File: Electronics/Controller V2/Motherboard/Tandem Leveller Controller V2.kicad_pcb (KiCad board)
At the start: 2 copper layers, 13 parts, among them J1 Conn_01x08, J2 Conn_01x10, J3 GNSS, U2 simpleRTK2B

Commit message: WIP
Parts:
- added C1: 100n, Capacitor_SMD:C_0805_2012Metric, F.Cu at (250.4, 66.3)
- added C10: 100n, Capacitor_SMD:C_0805_2012Metric, F.Cu at (102.7, -32.0)
- added C11: 560u, Capacitor_SMD:CP_Elec_10x10.5, F.Cu at (117.4, -65.3)
- added C12: 560u, Capacitor_SMD:CP_Elec_10x10.5, F.Cu at (117.4, -53.2)
- added C2: 100n, Capacitor_SMD:C_0805_2012Metric, F.Cu at (250.4, 69.3)
- added C3: 100n, Capacitor_SMD:C_0805_2012Metric, F.Cu at (99.2, -7.16)
- added C4: 100n, Capacitor_SMD:C_0805_2012Metric, F.Cu at (99.2, -4.15)
- added C5: 680u, Capacitor_SMD:CP_Elec_10x10.5, F.Cu at (117.4, -77.3)
- added C6: 220u, Capacitor_SMD:CP_Elec_8x6.5, F.Cu at (98.4, -41.4)
- added C7: 1729034, Capacitor_SMD:CP_Elec_6.3x5.9, F.Cu at (145.4, -79.3)
- added C8: 1729034, Capacitor_SMD:CP_Elec_6.3x5.9, F.Cu at (145.4, -71.2)
- added C9: 100n, Capacitor_SMD:C_0805_2012Metric, F.Cu at (102.7, -35.0)
- added D1: APTD1608SECK, Diode_SMD:D_0603_1608Metric, F.Cu at (102.5, -29.2)
- added D2: B360A-13-F, Diode_SMD:D_SMA, F.Cu at (96.4, -34.2)
- added D3: PDS760-13, Diode_SMD:D_PowerDI-5, F.Cu at (118.8, -44.4)
- added D4: PDS760-13, Diode_SMD:D_PowerDI-5, F.Cu at (118.8, -38.8)
- added F1: 10A, Britishideas:5x20 Fuse Holder, F.Cu at (126.0, -38.0)
- added J14: TABLET 1 PWR, Connector_BarrelJack:BarrelJack_Wuerth_6941xx301002, F.Cu at (130.1, -54.0)
- added J15: TABLET 2 PWR, Connector_BarrelJack:BarrelJack_Wuerth_6941xx301002, F.Cu at (142.4, -54.0)
- added J4: TERM, Connector_PinHeader_2.54mm:PinHeader_1x02_P2.54mm_Vertical, F.Cu at (94.7, -6.34)
- added J5: Pulse_J0011D01BNL, EmSA:Pulse_J0011D01BNL, F.Cu at (240.0, 62.3)
- added J6: CAN, Connector_Dsub:DSUB-9_Male_Vertical_P2.77x2.84mm, F.Cu at (107.5, -19.9)
- added J7: Pulse_J0011D01BNL, EmSA:Pulse_J0011D01BNL, F.Cu at (258.8, 62.3)
- added L1: ACT1210-510-2P-TL00, EmSA:ACT1210-510-2P-TL00, F.Cu at (108.4, -6.86)
- added L2: 33uH, Britishideas:MWSA0603S-330MT, F.Cu at (116.1, -32.1)
- added L3: MWSA1206S-470MT, Britishideas:MWSA1206S-470MT, F.Cu at (126.7, -76.5)
- added L4: MWSA1206S-470MT, Britishideas:MWSA1206S-470MT, F.Cu at (126.7, -62.8)
- added R1: 1k, Resistor_SMD:R_0805_2012Metric, F.Cu at (237.2, 66.2)
- added R10: 1k, Resistor_SMD:R_0805_2012Metric, F.Cu at (246.0, 69.2)
- added R11: 1k, Resistor_SMD:R_0805_2012Metric, F.Cu at (246.0, 72.1)
- added R12: 330, Resistor_SMD:R_0805_2012Metric, F.Cu at (112.2, -45.8)
- added R13: 10k, Resistor_SMD:R_0805_2012Metric, F.Cu at (103.6, -7.19)
- added R14: 120, Resistor_SMD:R_0805_2012Metric, F.Cu at (103.6, -4.24)
- added R15: 3k, Resistor_SMD:R_0805_2012Metric, F.Cu at (112.2, -42.8)
- added R16: 3k, Resistor_SMD:R_0805_2012Metric, F.Cu at (112.2, -39.9)
- added R17: 1k, Resistor_SMD:R_0805_2012Metric, F.Cu at (246.0, 75.1)
- added R18: 18k, Resistor_SMD:R_0805_2012Metric, F.Cu at (112.2, -36.9)
- added R19: 1k5, Resistor_SMD:R_0805_2012Metric, F.Cu at (112.2, -34.0)
- added R2: 1k, Resistor_SMD:R_0805_2012Metric, F.Cu at (237.2, 69.2)
- added R20: 18k, Resistor_SMD:R_0805_2012Metric, F.Cu at (112.2, -31.0)
- added R21: 1k5, Resistor_SMD:R_0805_2012Metric, F.Cu at (112.2, -28.1)
- added R3: 1k, Resistor_SMD:R_0805_2012Metric, F.Cu at (237.2, 72.1)
- added R4: 1k, Resistor_SMD:R_0805_2012Metric, F.Cu at (237.2, 75.1)
- added R5: 1k, Resistor_SMD:R_0805_2012Metric, F.Cu at (241.6, 66.2)
- added R6: 1k, Resistor_SMD:R_0805_2012Metric, F.Cu at (241.6, 69.2)
- added R7: 1k, Resistor_SMD:R_0805_2012Metric, F.Cu at (241.6, 72.1)
- added R8: 1k, Resistor_SMD:R_0805_2012Metric, F.Cu at (241.6, 75.1)
- added R9: 1k, Resistor_SMD:R_0805_2012Metric, F.Cu at (246.0, 66.2)
- added U10: LM2587S-ADJ/NOPB, Package_TO_SOT_SMD:TO-263-5_TabPin6, F.Cu at (103.1, -52.5)
- added U3: Adafruit BNO085, Britishideas:Adafruit_BNO085, F.Cu at (25.2, 63.8)
- added U4: ~, Britishideas:Teensy_4.1, F.Cu at (198.6, 43.8)
- added U5: ~, Britishideas:Teensy_4.1, F.Cu at (217.7, 43.8)
- added U6: TJA1462ATK-0Z, EmSA:HVSON8_0_65mm, F.Cu at (117.1, -5.18)
- added U7: PESD2CANFD24V-TR, Package_TO_SOT_SMD:SOT-23, F.Cu at (113.4, -6.44)
- added U8: LM2596S-5, Package_TO_SOT_SMD:TO-263-5_TabPin3, F.Cu at (103.1, -77.2)
- added U9: LM2587S-ADJ/NOPB, Package_TO_SOT_SMD:TO-263-5_TabPin6, F.Cu at (103.1, -64.8)
- moved H1 63.1 mm to (123.1, 91.2)
- moved H2 63.1 mm to (177.6, 91.2)
- moved H3 63.1 mm to (177.6, 155.7)
- moved H4 63.1 mm to (123.1, 155.7)
- moved J1 63.1 mm to (175.1, 101.2)
- moved J2 63.1 mm to (133.1, 123.2)
- moved U1 63.1 mm to (162.9, 90.7)
- moved H7 22.5 mm to (28.5, 155.1)
- moved U2 22.5 mm to (38.0, 93.1)
- moved H5 22.5 mm to (28.5, 94.6)
- moved H8 22.5 mm to (103.0, 155.1)
- moved J3 22.5 mm to (92.5, 145.6)
- moved H6 22.5 mm to (103.0, 94.6)
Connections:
- U1 pad 1: /Valves/VALVE_A_DIR -> /MCUs/VALVE_A_DIR
- U1 pad 2: /Valves/VALVE_A_PWM -> /MCUs/VALVE_A_PWM

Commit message: Added AMP connectors. Working on PCB layout.
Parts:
- added J8: 776180-1, Britishideas:776180-1 AMPHENOL AMP 35pos, F.Cu at (221.9, 114.0)
- added J9: 776279-1, Britishideas:776279-1 AMPHENOL AMP 8pos, F.Cu at (221.9, 36.7)
- moved U5 312.9 mm to (527.5, 87.9), turned to 180 degrees
- moved C1 296.9 mm to (547.3, 61.1)
- moved C2 296.9 mm to (547.3, 64.1)
- moved C3 296.9 mm to (396.1, -12.4)
- moved C4 296.9 mm to (396.1, -9.35)
- moved C6 296.9 mm to (395.3, -46.6)
- moved H5 296.9 mm to (325.4, 89.4)
- moved H7 296.9 mm to (325.4, 149.9)
- moved J6 296.9 mm to (404.4, -25.1)
- moved L1 296.9 mm to (405.3, -12.1)
- moved R1 296.9 mm to (534.1, 61.0)
- moved R13 296.9 mm to (400.5, -12.4)
- moved R14 296.9 mm to (400.5, -9.44)
- moved R2 296.9 mm to (534.1, 64.0)
- moved R3 296.9 mm to (534.1, 66.9)
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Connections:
- net /CAN/CAN_H renamed /CAN_H
- net /CAN/CAN_L renamed /CAN_L
- J2 pad 2: /Valves/VALVE_B_MA -> /VALVE_B_MA
- J2 pad 3: /Valves/VALVE_B_MB -> /VALVE_B_MB
- J2 pad 4: /Valves/VALVE_C_MA -> /VALVE_C_MA
- J2 pad 5: /Valves/VALVE_C_MB -> /VALVE_C_MB
- J2 pad 6: /Valves/VALVE_D_MA -> /VALVE_D_MA
- J2 pad 7: /Valves/VALVE_D_MB -> /VALVE_D_MB
- J2 pad 8: /Valves/VALVE_E_MA -> /VALVE_E_MA
- J2 pad 9: /Valves/VALVE_E_MB -> /VALVE_E_MB
- U1 pad 6: /Valves/VALVE_A_MA -> /VALVE_A_MA
- U1 pad 7: /Valves/VALVE_A_MB -> /VALVE_A_MB
- U4 pad 28: /MCUs/GPIO_C4 -> /GPIO_C4
- U4 pad 29: /MCUs/GPIO_C3 -> /GPIO_C3
- U4 pad 30: /MCUs/GPIO_C2 -> /GPIO_C2
- U4 pad 31: /MCUs/GPIO_C1 -> /GPIO_C1
- U5 pad 46: +3V3 -> unconnected-(U5-3V3-Pad46)
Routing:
- net +BATT: track 0.00 -> 34.1 mm
- net +12V: track 0.00 -> 10.0 mm

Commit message: Working on V2 controller PCB.
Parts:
- added H10: MountingHole, MountingHole:MountingHole_3.2mm_M3, F.Cu at (30.5, 149.5)
- added H11: MountingHole, MountingHole:MountingHole_3.2mm_M3, F.Cu at (30.5, 27.5)
- added H12: MountingHole, MountingHole:MountingHole_3.2mm_M3, F.Cu at (246.0, 27.5)
- added H9: MountingHole, MountingHole:MountingHole_3.2mm_M3, F.Cu at (246.0, 149.5)
- moved C2 435.6 mm to (117.6, 135.1), turned to -90 degrees
- moved R17 432.5 mm to (117.6, 148.3), turned to -90 degrees
- moved R9 419.9 mm to (123.2, 72.5), turned to 180 degrees
- moved C1 416.6 mm to (137.4, 135.2), turned to -90 degrees
- moved R7 415.4 mm to (123.2, 74.6), turned to 180 degrees
- moved U5 408.9 mm to (119.0, 69.8), turned to 0 degrees
- moved R8 408.6 mm to (137.5, 148.3), turned to -90 degrees
- moved J7 395.1 mm to (131.6, 135.4)
- moved R1 394.5 mm to (143.2, 113.6), turned to 180 degrees
- moved R3 394.3 mm to (143.2, 118.2), turned to 180 degrees
- moved R4 394.2 mm to (143.2, 120.3), turned to 180 degrees
- moved R2 393.8 mm to (143.2, 111.5), turned to 180 degrees
- moved R10 386.5 mm to (158.4, 102.5)
- moved R11 386.0 mm to (158.4, 100.4)
- moved R5 385.1 mm to (158.5, 123.3)
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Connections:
- U4 pad 44: /MCUs/CAN_TX -> /CAN/CAN_TX
- U4 pad 45: /MCUs/CAN_RX -> /CAN/CAN_RX
- U5 pad 44: /MCUs/CAN_TX -> unconnected-(U5-GPIO22_CTX1-Pad44)
- U5 pad 45: /MCUs/CAN_RX -> unconnected-(U5-GPIO23_CRX1-Pad45)
- U6 pad 1: /MCUs/CAN_TX -> /CAN/CAN_TX
- U6 pad 4: /MCUs/CAN_RX -> /CAN/CAN_RX
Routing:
- net +BATT: track 34.1 -> 0.00 mm
- net +12V: track 10.0 -> 0.00 mm
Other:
- board outline added: 230.5 x 129 mm
- board text added: "10A"
- board text added: "16V OUT"
- board text added: "CAN BUS"
- board text added: "PRIMARY"
- board text added: "PWR"
- board text added: "SECONDARY"
- board text added: "TANDEM LEVELLER CONTROLLER V2.0 (C) ANDY@BRITISHIDEAS.COM 2026"

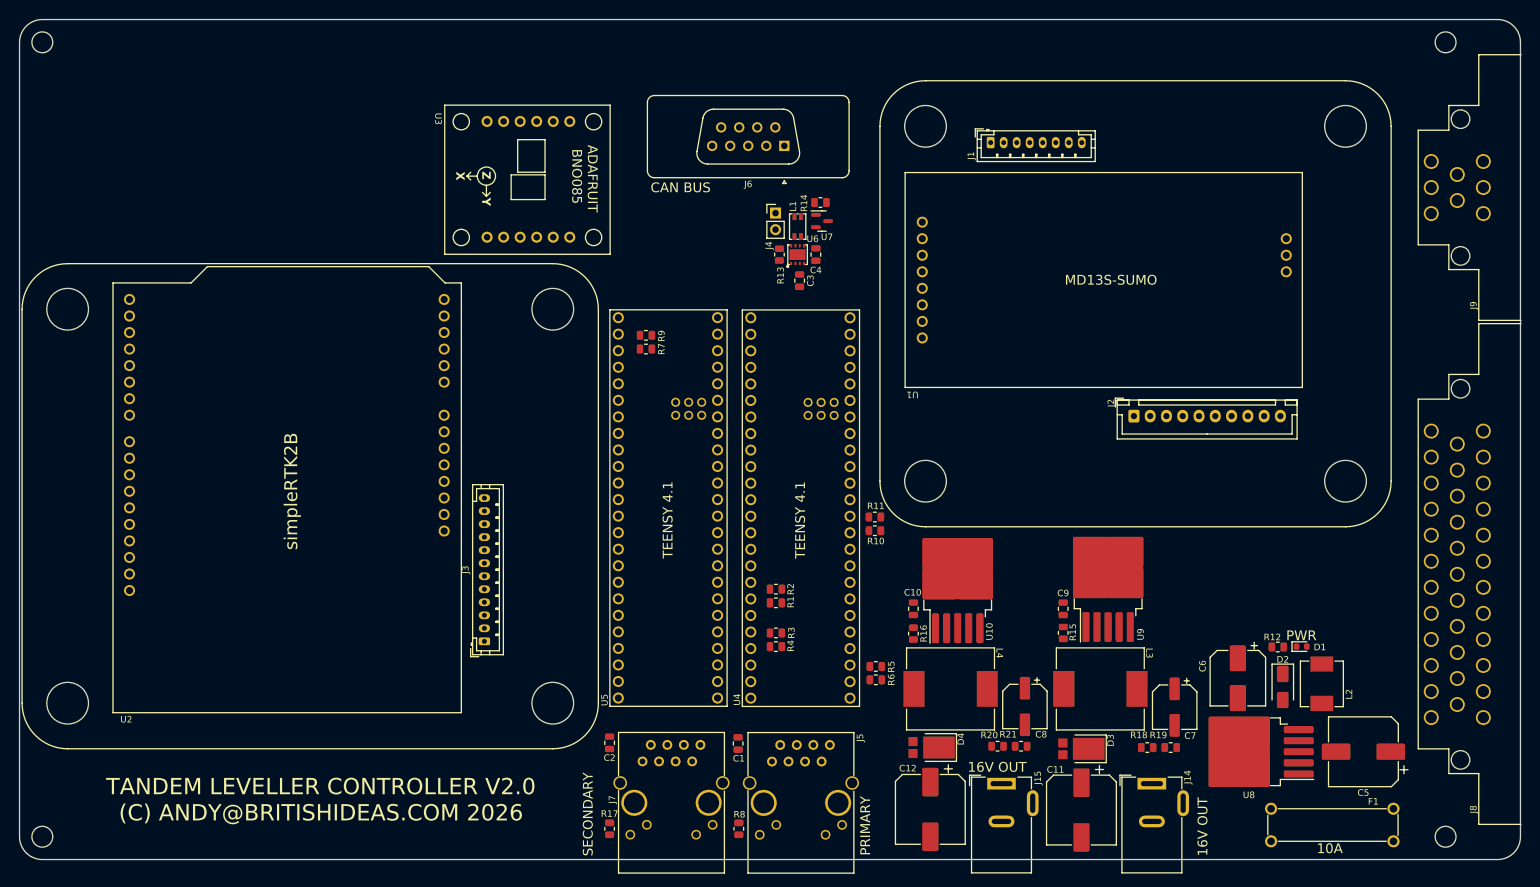
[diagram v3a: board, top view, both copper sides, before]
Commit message: Added missing ground connection. Working on PCB layout.
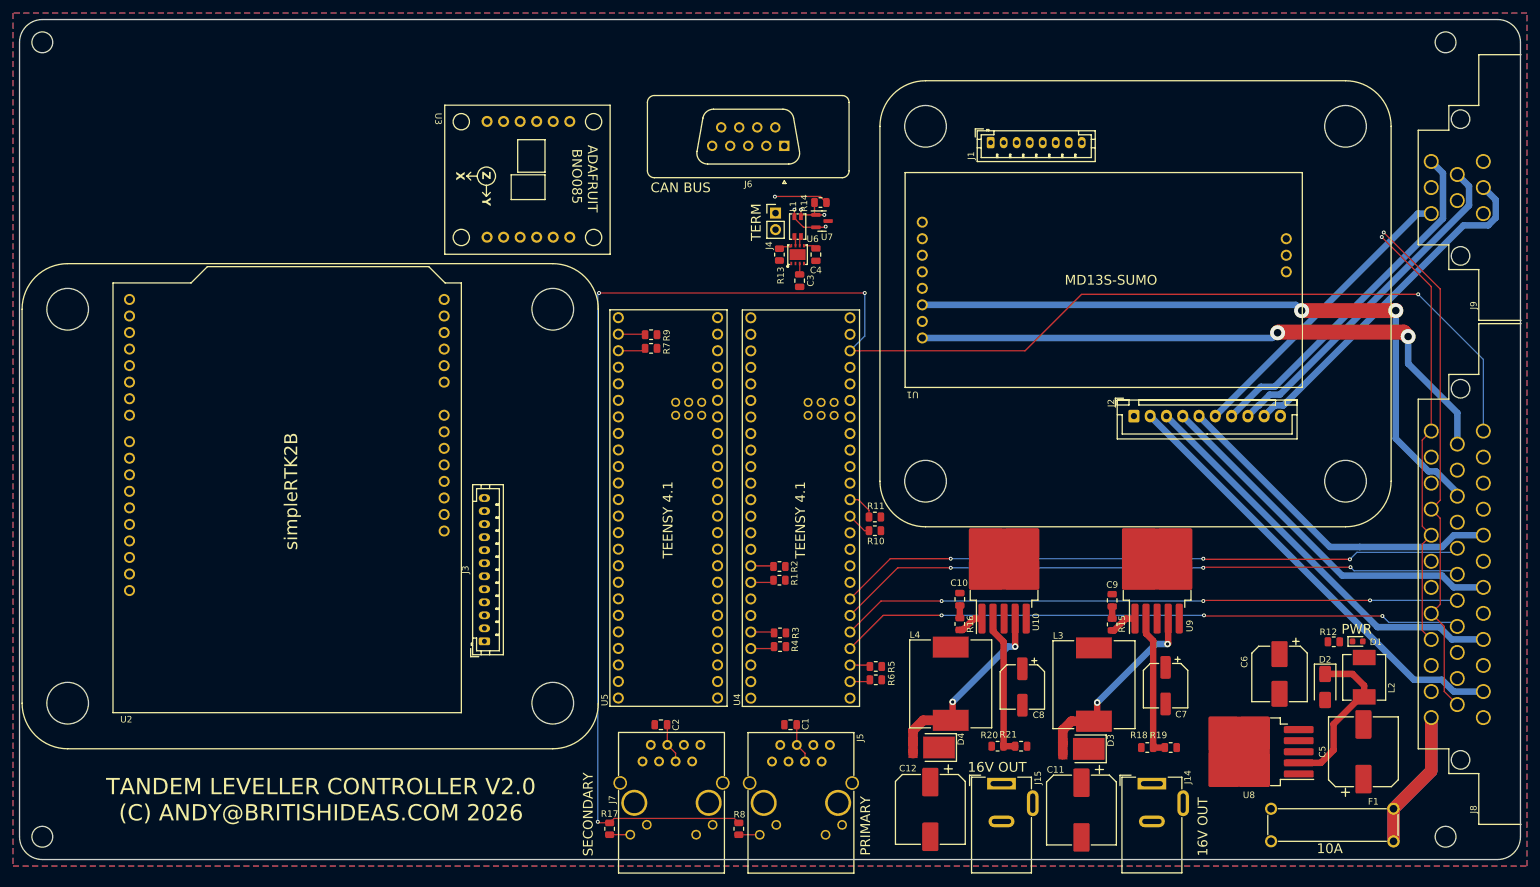
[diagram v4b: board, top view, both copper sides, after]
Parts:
- moved L3 9.14 mm to (192.0, 120.5), turned to -90 degrees
- moved R12 8.64 mm to (228.8, 119.6)
- moved D1 8.64 mm to (232.5, 119.5)
- moved C1 8.54 mm to (145.4, 132.3), turned to 0 degrees
- moved L4 8.54 mm to (170.0, 120.4), turned to -90 degrees
- moved C2 8.36 mm to (125.5, 132.3), turned to 0 degrees
- moved C9 7.63 mm to (194.8, 113.2)
- moved R15 7.63 mm to (194.8, 116.9)
- moved U9 7.63 mm to (201.7, 108.3)
- moved U10 7.28 mm to (178.2, 108.3)
- moved C10 7.28 mm to (171.4, 113.0)
- moved R16 7.28 mm to (171.4, 116.8)
- moved L2 6.58 mm to (233.5, 128.0)
- moved D2 6.50 mm to (227.5, 126.5)
- moved C6 6.43 mm to (220.5, 124.5)
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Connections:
- C5 pad 2: Net-(D2-A) -> GND
- C6 pad 2: Net-(D2-A) -> GND
- D2 pad 2: Net-(D2-A) -> GND
- J8 pad 16: /GPIO_C1 -> /GPIO_C4
- J8 pad 17: /GPIO_C2 -> /GPIO_C3
- J8 pad 18: /GPIO_C3 -> /GPIO_C2
- J8 pad 19: /GPIO_C4 -> /GPIO_C1
- J8 pad 34: GND -> +12V
- J8 pad 35: GND -> +3V3
- U4 pad 38: /GNSS/GPIO_G4 -> /GNSS/GPIO_G1
- U4 pad 39: /GNSS/GPIO_G3 -> /GNSS/GPIO_G2
- U4 pad 40: /GNSS/GPIO_G2 -> /GNSS/GPIO_G3
- U4 pad 41: /GNSS/GPIO_G1 -> /GNSS/GPIO_G4
- U8 pad 3: Net-(D2-A) -> GND
- U8 pad 5: Net-(D2-A) -> GND
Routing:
- net +3V3: track 0.00 -> 270.2 mm, vias 0 -> 4
- net /VALVE_A_MA: track 0.00 -> 197.9 mm, vias 0 -> 2
- net /CAN_L: track 0.00 -> 185.5 mm, vias 0 -> 3
- net /CAN_H: track 0.00 -> 180.7 mm, vias 0 -> 3
- net /VALVE_A_MB: track 0.00 -> 169.5 mm, vias 0 -> 2
- net /VALVE_B_MA: track 0.00 -> 138.2 mm
- net /VALVE_B_MB: track 0.00 -> 125.7 mm
- net /VALVE_C_MA: track 0.00 -> 114.1 mm
- net /VALVE_D_MB: track 0.00 -> 109.1 mm
- net /VALVE_E_MB: track 0.00 -> 107.2 mm
- net /VALVE_E_MA: track 0.00 -> 105.7 mm
- net /VALVE_C_MB: track 0.00 -> 105.5 mm
- net /GPIO_C2: track 0.00 -> 96.8 mm, vias 0 -> 3
- net /GPIO_C1: track 0.00 -> 96.6 mm, vias 0 -> 3
- net /GPIO_C4: track 0.00 -> 96.1 mm, vias 0 -> 3
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- added copper zone on In2.Cu, net +12V
- added copper zone on In2.Cu, net +5V
- added copper zone on In2.Cu, net /Power/16V_1
- added copper zone on In2.Cu, net /Power/16V_2
- added copper zone on B.Cu, net GND
- added copper zone on F.Cu, net GND
- added copper zone on In1.Cu, net GND
- added copper zone on In3.Cu, net GND
- added copper zone on In4.Cu, net GND
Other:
- copper layers 2 -> 6
- board text added: "TERM"

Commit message: Working on motherboard layout. Added SMA adapters to GNSS daughterboard. Generated CAD files.
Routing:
- net /GNSS/GNSS_A_TX: track 0.00 -> 146.5 mm, vias 0 -> 5
- net /GNSS/GNSS_A_RX: track 0.00 -> 138.0 mm, vias 0 -> 4
- net /IMU/~{IMU_RST}: track 0.00 -> 129.0 mm, vias 0 -> 2
- net /IMU/~{IMU_INT}: track 0.00 -> 128.8 mm, vias 0 -> 2
- net /IMU/IMU_SCK: track 0.00 -> 118.6 mm, vias 0 -> 2
- net /IMU/IMU_MISO: track 0.00 -> 99.4 mm, vias 0 -> 2
- net /Valves/VALVE_E_PWM: track 0.00 -> 92.6 mm, vias 0 -> 3
- net +12V: track 0.00 -> 89.0 mm, vias 0 -> 31
- net /Valves/VALVE_E_DIR: track 0.00 -> 88.8 mm, vias 0 -> 3
- net /Valves/VALVE_D_PWM: track 0.00 -> 84.4 mm, vias 0 -> 3
- net /GNSS/GNSS_C_TX: track 0.00 -> 80.4 mm, vias 0 -> 2
- net /Valves/VALVE_D_DIR: track 0.00 -> 79.9 mm, vias 0 -> 3
- net /IMU/IMU_MOSI: track 0.00 -> 78.7 mm, vias 0 -> 1
- net /IMU/~{IMU_CS}: track 0.00 -> 78.2 mm, vias 0 -> 1
- net /Valves/VALVE_C_PWM: track 0.00 -> 75.6 mm, vias 0 -> 3
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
